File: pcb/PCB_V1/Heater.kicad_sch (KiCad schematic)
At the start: 8 parts, among them J601 PTC + / switched - (3.5 mm), Q601 NTMFS5C628NLT1G, U601 UCC27524ADR

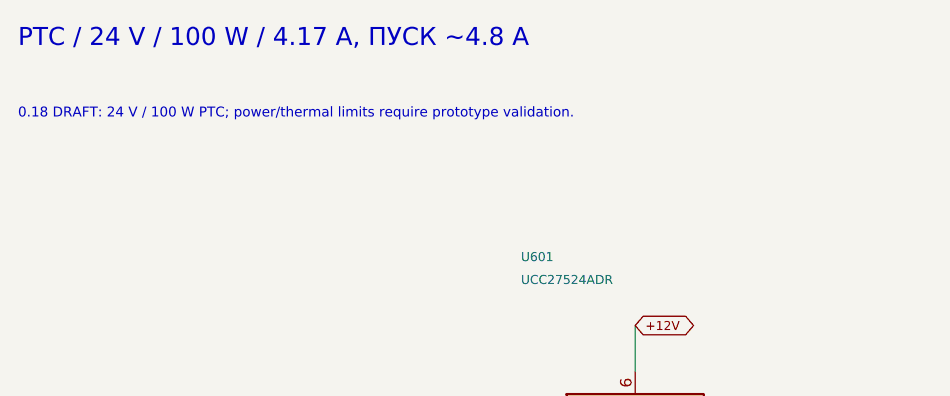
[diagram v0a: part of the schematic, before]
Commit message: pcb: revision 0.20 cost-down with new footprints and placement
- RTC: DS3231MZ replaced by NXP PCF8563T/5 with an Epson FC-135 crystal
  (CL 12.5 pF), C304 18 pF C0G on OSCI, BAT54C supply OR (D303) and R307
  1k from the CR2032.
- Boost switches Q711/Q721: AOS AOD66923 (DPAK) on a project footprint
  that keeps the S1/2/3 G4 D5 numbering; diodes D711/D721: Vishay SS5P10
  (TO-277A).
- L101 cjiang FXL0630-100-M and L902 PROD PSPMAA0604-220M-ANP on the
  KiCad FXL0630 land.
- LED switch areas and the RTC cluster re-placed (29 parts moved);
  ERC 0, DRC 0, 340 unrouted links.
- Checks, price/JLC snapshots v20, reports, placement images and docs
  updated: USD 31.62 per board (29.52 for five boards).

Co-Authored-By: Claude Opus 5.5 <noreply@anthropic.com>
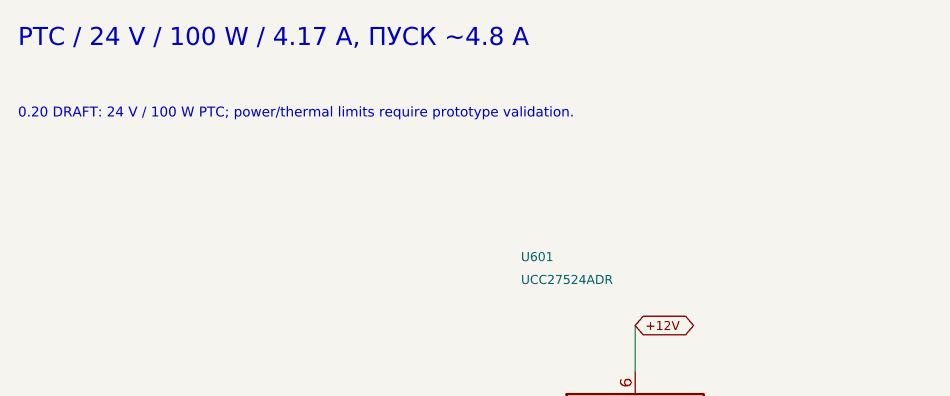
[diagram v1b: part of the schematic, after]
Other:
- note added: "0.20 DRAFT: 24 V / 100 W PTC; power/thermal limits require prototype validation."
- note removed: "0.18 DRAFT: 24 V / 100 W PTC; power/thermal limits require prototype validation."
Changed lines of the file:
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@@
 		(title "05 - PTC heater switch (24 V)")
 		(date "2026-09-29")
-		(rev "0.18-DRAFT")
+		(rev "0.20-DRAFT")
 		(company "GrowBox controller")
 		(comment 1 "Simplified prototype; unrouted; hardware qualification pending")
@@
 		)
 	)
-	(text "0.18 DRAFT: 24 V / 100 W PTC; power/thermal limits require prototype validation."
+	(text "0.20 DRAFT: 24 V / 100 W PTC; power/thermal limits require prototype validation."
 		(exclude_from_sim no)
 		(at 20.32 24.13 0)
